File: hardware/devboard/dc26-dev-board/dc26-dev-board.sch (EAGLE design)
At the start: 88 parts, among them CN1 JST, IC1 STM32F411RET6, M10 STM32-Breakout-2, U1 ESP-WROOM-32, Y1 ABL-8.000MHZ-B2

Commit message: ready for review again.
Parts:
- renumbered U$3 to CHARGING_CIRCUT, U$6 to RESET_BUTTON
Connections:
- net PA10 renamed USART1_RX
- net PA9 renamed USART1_TX

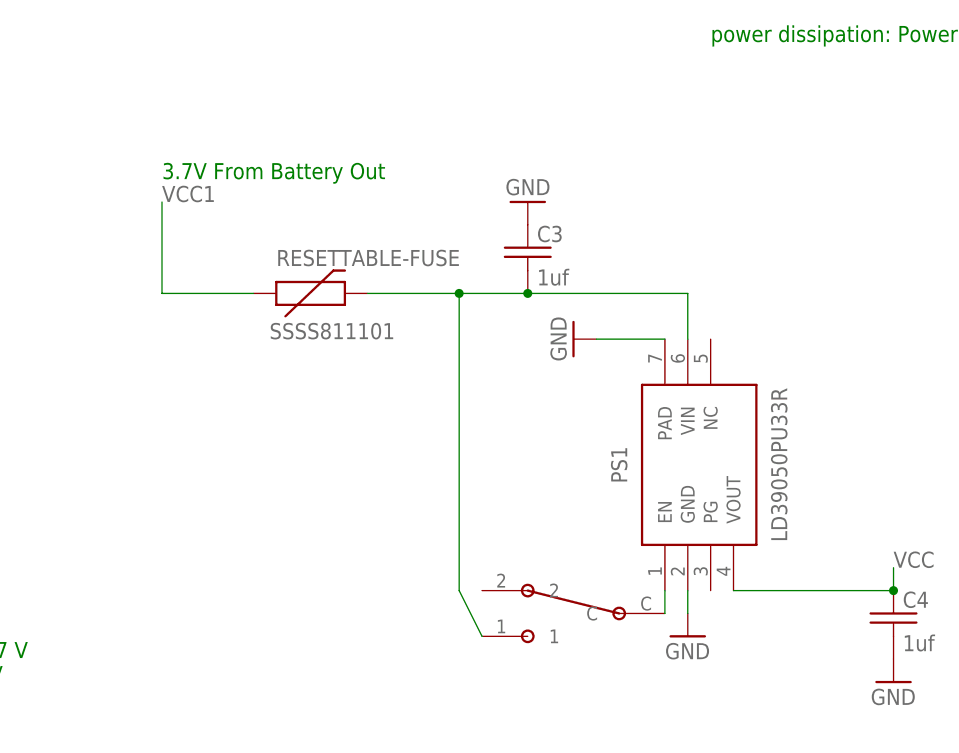
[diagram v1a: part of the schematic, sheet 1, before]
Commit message: swapped out voltage regulator for one that supports 1A rather than just .5A
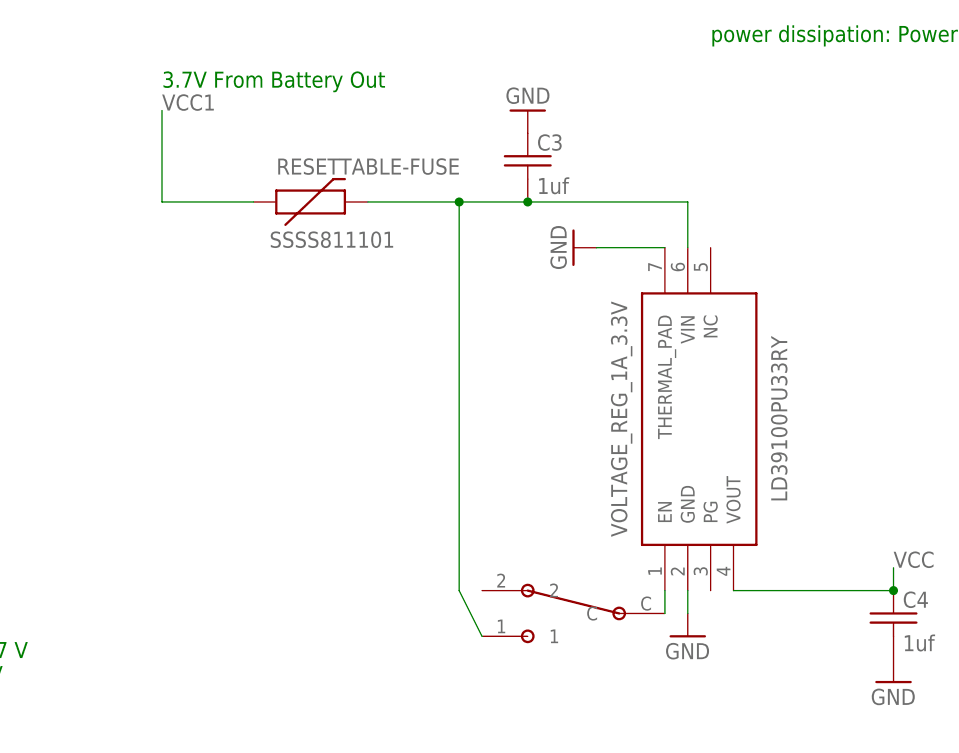
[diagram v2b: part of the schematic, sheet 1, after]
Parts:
- removed PS1: LD39050PU33R, dc-26:LD39050PU33R
- added VOLTAGE_REG_1A_3.3V: LD39100PU33RY, dc-26:LD39100PU33RY
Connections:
- net GND: now also VOLTAGE_REG_1A_3.3V.GND, VOLTAGE_REG_1A_3.3V.THERMAL_PAD; no longer PS1.GND, PS1.PAD
- net VCC: now also VOLTAGE_REG_1A_3.3V.VOUT; no longer PS1.VOUT
- net VIN: now also VOLTAGE_REG_1A_3.3V.VIN; no longer PS1.VIN
- net VIN-EN: now also VOLTAGE_REG_1A_3.3V.EN; no longer PS1.EN
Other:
- moved on the sheet: C3, RESETTABLE-FUSE
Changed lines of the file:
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@@
 <part name="C17" library="dc-26" deviceset="C-US" device="C0805" value="4.7uF"/>
 <part name="GND65" library="dc-26" deviceset="GND" device=""/>
-<part name="PS1" library="dc-26" deviceset="LD39050PU33R" device=""/>
 <part name="GND7" library="dc-26" deviceset="GND" device=""/>
 <part name="R5" library="dc-26" deviceset="RESISTOR" device="0805-RES" value="10K"/>
@@
 <part name="GND69" library="dc-26" deviceset="GND" device=""/>
 <part name="R8" library="dc-26" deviceset="RESISTOR" device="0805-RES" value="4K7"/>
+<part name="VOLTAGE_REG_1A_3.3V" library="dc-26" deviceset="LD39100PU33RY" device=""/>
 </parts>
 <sheets>
@@
 <text x="43.18" y="91.44" size="1.778" layer="91">Battery, USB, ST-LINK Power Out</text>
 <text x="172.72" y="114.3" size="1.778" layer="91">power dissipation: Power Rule: P = I × V</text>
-<text x="111.76" y="99.06" size="1.778" layer="91">3.7V From Battery Out</text>
+<text x="111.76" y="109.22" size="1.778" layer="91">3.7V From Battery Out</text>
 <text x="81.28" y="43.18" size="1.778" layer="91">VCC0 = 5V
 VCC 1 = 3.7 V
@@
 <instance part="R2" gate="G$1" x="-7.62" y="81.28" rot="R90"/>
 <instance part="R3" gate="G$1" x="27.94" y="71.12" rot="R90"/>
-<instance part="RESETTABLE-FUSE" gate="G$1" x="127" y="86.36"/>
+<instance part="RESETTABLE-FUSE" gate="G$1" x="127" y="96.52"/>
 <instance part="U$5" gate="G$1" x="157.48" y="50.8"/>
-<instance part="C3" gate="G$1" x="152.4" y="91.44"/>
+<instance part="C3" gate="G$1" x="152.4" y="101.6"/>
 <instance part="C4" gate="G$1" x="193.04" y="50.8"/>
-<instance part="GND6" gate="1" x="152.4" y="96.52" rot="R180"/>
+<instance part="GND6" gate="1" x="152.4" y="106.68" rot="R180"/>
 <instance part="GND" gate="1" x="193.04" y="43.18"/>
 <instance part="GND8" gate="1" x="170.18" y="48.26"/>
-<instance part="PS1" gate="G$1" x="167.64" y="53.34" rot="R90"/>
-<instance part="GND7" gate="1" x="157.48" y="81.28" rot="R270"/>
+<instance part="GND7" gate="1" x="157.48" y="91.44" rot="R270"/>
 <instance part="U$2" gate="G$1" x="27.94" y="33.02" rot="R180"/>
 <instance part="U$4" gate="G$1" x="15.24" y="2.54"/>
 <instance part="GND5" gate="1" x="43.18" y="-15.24"/>
 <instance part="GND9" gate="1" x="43.18" y="40.64" rot="R180"/>
+<instance part="VOLTAGE_REG_1A_3.3V" gate="G$1" x="167.64" y="53.34" rot="R90"/>
 </instances>
 <busses>
@@
 </segment>
 <segment>
-<pinref part="PS1" gate="G$1" pin="GND"/>
 <wire x1="170.18" y1="53.34" x2="170.18" y2="50.8" width="0.1524" layer="91"/>
 <pinref part="GND8" gate="1" pin="GND"/>
-</segment>
-<segment>
-<pinref part="PS1" gate="G$1" pin="PAD"/>
-<wire x1="167.64" y1="81.28" x2="160.02" y2="81.28" width="0.1524" layer="91"/>
-<pinref part="GND7" gate="1" pin="GND"/>
+<pinref part="VOLTAGE_REG_1A_3.3V" gate="G$1" pin="GND"/>
 </segment>
 <segment>
@@
 <wire x1="43.18" y1="30.48" x2="43.18" y2="38.1" width="0.1524" layer="91"/>
 <pinref part="GND9" gate="1" pin="GND"/>
+</segment>
+<segment>
+<pinref part="VOLTAGE_REG_1A_3.3V" gate="G$1" pin="THERMAL_PAD"/>
+<pinref part="GND7" gate="1" pin="GND"/>
+<wire x1="167.64" y1="91.44" x2="160.02" y2="91.44" width="0.1524" layer="91"/>
 </segment>
 </net>
@@
 <segment>
 <pinref part="RESETTABLE-FUSE" gate="G$1" pin="1"/>
-<wire x1="111.76" y1="96.52" x2="111.76" y2="86.36" width="0.1524" layer="91"/>
-<wire x1="111.76" y1="86.36" x2="121.92" y2="86.36" width="0.1524" layer="91"/>
-<label x="111.76" y="96.52" size="1.778" layer="95"/>
+<wire x1="111.76" y1="106.68" x2="111.76" y2="96.52" width="0.1524" layer="91"/>
+<wire x1="111.76" y1="96.52" x2="121.92" y2="96.52" width="0.1524" layer="91"/>
+<label x="111.76" y="106.68" size="1.778" layer="95"/>
 </segment>
 </net>
@@
 <pinref part="C3" gate="G$1" pin="2"/>
 <pinref part="RESETTABLE-FUSE" gate="G$1" pin="2"/>
-<wire x1="152.4" y1="86.36" x2="144.78" y2="86.36" width="0.1524" layer="91"/>
-<junction x="152.4" y="86.36"/>
+<wire x1="152.4" y1="96.52" x2="144.78" y2="96.52" width="0.1524" layer="91"/>
+<junction x="152.4" y="96.52"/>
 <pinref part="U$5" gate="G$1" pin="1"/>
-<wire x1="144.78" y1="86.36" x2="134.62" y2="86.36" width="0.1524" layer="91"/>
+<wire x1="144.78" y1="96.52" x2="134.62" y2="96.52" width="0.1524" layer="91"/>
 <wire x1="147.32" y1="48.26" x2="144.78" y2="53.34" width="0.1524" layer="91"/>
-<wire x1="144.78" y1="53.34" x2="144.78" y2="86.36" width="0.1524" layer="91"/>
-<junction x="144.78" y="86.36"/>
-<pinref part="PS1" gate="G$1" pin="VIN"/>
-<wire x1="152.4" y1="86.36" x2="170.18" y2="86.36" width="0.1524" layer="91"/>
-<wire x1="170.18" y1="86.36" x2="170.18" y2="81.28" width="0.1524" layer="91"/>
+<wire x1="144.78" y1="53.34" x2="144.78" y2="96.52" width="0.1524" layer="91"/>
+<junction x="144.78" y="96.52"/>
+<wire x1="152.4" y1="96.52" x2="170.18" y2="96.52" width="0.1524" layer="91"/>
+<pinref part="VOLTAGE_REG_1A_3.3V" gate="G$1" pin="VIN"/>
+<wire x1="170.18" y1="91.44" x2="170.18" y2="96.52" width="0.1524" layer="91"/>
 </segment>
 </net>
@@
 <wire x1="193.04" y1="53.34" x2="193.04" y2="55.88" width="0.1524" layer="91"/>
 <label x="193.04" y="55.88" size="1.778" layer="95"/>
-<pinref part="PS1" gate="G$1" pin="VOUT"/>
 <wire x1="175.26" y1="53.34" x2="193.04" y2="53.34" width="0.1524" layer="91"/>
 <junction x="193.04" y="53.34"/>
+<pinref part="VOLTAGE_REG_1A_3.3V" gate="G$1" pin="VOUT"/>
 </segment>
 </net>
@@
 <segment>
 <pinref part="U$5" gate="G$1" pin="C"/>
-<pinref part="PS1" gate="G$1" pin="EN"/>
 <wire x1="167.64" y1="50.8" x2="167.64" y2="53.34" width="0.1524" layer="91"/>
-</segment>
-</net>
+<pinref part="VOLTAGE_REG_1A_3.3V" gate="G$1" pin="EN"/>
+</segment>
+</net>

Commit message: inital board layout
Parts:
- renumbered ESP32-PROGRAM-HEADER to ESP32PH, U$2 to USB, U$4 to LINK1, VOLTAGE_REG_1A_3.3V to VDO
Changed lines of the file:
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@@
 <part name="C1" library="dc-26" deviceset="C-US" device="C0805" value="4.7uF"/>
 <part name="C2" library="dc-26" deviceset="C-US" device="C0805" value="4.7uf"/>
-<part name="U$2" library="dc-26" deviceset="DX4R005JJ2" device="DX4R005JJ2"/>
+<part name="USB" library="dc-26" deviceset="DX4R005JJ2" device="DX4R005JJ2"/>
 <part name="CHARGING_CIRCUT" library="dc-26" deviceset="DS21984E" device="" value="MCP73831"/>
 <part name="GND1" library="dc-26" deviceset="GND" device=""/>
@@
 <part name="GND4" library="dc-26" deviceset="GND" device=""/>
 <part name="LED1" library="dc-26" deviceset="LED" device="1206" value="MF-LED-0603-GREEN"/>
-<part name="U$4" library="dc-26" deviceset="STLINK-V2-CONNECTOR" device=""/>
+<part name="LINK1" library="dc-26" deviceset="STLINK-V2-CONNECTOR" device=""/>
 <part name="GND5" library="dc-26" deviceset="GND" device=""/>
 <part name="RESETTABLE-FUSE" library="dc-26" deviceset="PTC" device="SMD" value="SSSS811101"/>
@@
 <part name="C13" library="dc-26" deviceset="C-US" device="C0805" value="10uF"/>
 <part name="GND13" library="dc-26" deviceset="GND" device=""/>
-<part name="ESP32-PROGRAM-HEADER" library="dc-26" deviceset="SERIAL_4" device=""/>
+<part name="ESP32PH" library="dc-26" deviceset="SERIAL_4" device=""/>
 <part name="Z1" library="dc-26" deviceset="CMDZ3L3_TR" device=""/>
 <part name="GND14" library="dc-26" deviceset="GND" device=""/>
@@
 <part name="GND69" library="dc-26" deviceset="GND" device=""/>
 <part name="R8" library="dc-26" deviceset="RESISTOR" device="0805-RES" value="4K7"/>
-<part name="VOLTAGE_REG_1A_3.3V" library="dc-26" deviceset="LD39100PU33RY" device=""/>
+<part name="VDO" library="dc-26" deviceset="LD39100PU33RY" device=""/>
 </parts>
 <sheets>
@@
 <instance part="GND8" gate="1" x="170.18" y="48.26"/>
 <instance part="GND7" gate="1" x="157.48" y="91.44" rot="R270"/>
-<instance part="U$2" gate="G$1" x="27.94" y="33.02" rot="R180"/>
-<instance part="U$4" gate="G$1" x="15.24" y="2.54"/>
+<instance part="USB" gate="G$1" x="27.94" y="33.02" rot="R180"/>
+<instance part="LINK1" gate="G$1" x="15.24" y="2.54"/>
 <instance part="GND5" gate="1" x="43.18" y="-15.24"/>
 <instance part="GND9" gate="1" x="43.18" y="40.64" rot="R180"/>
-<instance part="VOLTAGE_REG_1A_3.3V" gate="G$1" x="167.64" y="53.34" rot="R90"/>
+<instance part="VDO" gate="G$1" x="167.64" y="53.34" rot="R90"/>
 </instances>
 <busses>
@@
 <wire x1="170.18" y1="53.34" x2="170.18" y2="50.8" width="0.1524" layer="91"/>
 <pinref part="GND8" gate="1" pin="GND"/>
-<pinref part="VOLTAGE_REG_1A_3.3V" gate="G$1" pin="GND"/>
-</segment>
-<segment>
-<pinref part="U$4" gate="G$1" pin="GND"/>
+<pinref part="VDO" gate="G$1" pin="GND"/>
+</segment>
+<segment>
+<pinref part="LINK1" gate="G$1" pin="GND"/>
 <wire x1="25.4" y1="-7.62" x2="43.18" y2="-7.62" width="0.1524" layer="91"/>
 <wire x1="43.18" y1="-7.62" x2="43.18" y2="-12.7" width="0.1524" layer="91"/>
@@
 </segment>
 <segment>
-<pinref part="U$2" gate="G$1" pin="GND"/>
+<pinref part="USB" gate="G$1" pin="GND"/>
 <wire x1="33.02" y1="30.48" x2="43.18" y2="30.48" width="0.1524" layer="91"/>
 <wire x1="43.18" y1="30.48" x2="43.18" y2="38.1" width="0.1524" layer="91"/>
@@
 </segment>
 <segment>
-<pinref part="VOLTAGE_REG_1A_3.3V" gate="G$1" pin="THERMAL_PAD"/>
+<pinref part="VDO" gate="G$1" pin="THERMAL_PAD"/>
 <pinref part="GND7" gate="1" pin="GND"/>
 <wire x1="167.64" y1="91.44" x2="160.02" y2="91.44" width="0.1524" layer="91"/>
@@
 </segment>
 <segment>
-<pinref part="U$4" gate="G$1" pin="VCC"/>
+<pinref part="LINK1" gate="G$1" pin="VCC"/>
 <wire x1="25.4" y1="0" x2="43.18" y2="0" width="0.1524" layer="91"/>
 <wire x1="43.18" y1="0" x2="43.18" y2="5.08" width="0.1524" layer="91"/>
@@
 </segment>
 <segment>
-<pinref part="U$2" gate="G$1" pin="+5V"/>
+<pinref part="USB" gate="G$1" pin="+5V"/>
 <wire x1="33.02" y1="20.32" x2="40.64" y2="20.32" width="0.1524" layer="91"/>
 <label x="40.64" y="20.32" size="1.778" layer="95"/>
@@
 <junction x="144.78" y="96.52"/>
 <wire x1="152.4" y1="96.52" x2="170.18" y2="96.52" width="0.1524" layer="91"/>
-<pinref part="VOLTAGE_REG_1A_3.3V" gate="G$1" pin="VIN"/>
+<pinref part="VDO" gate="G$1" pin="VIN"/>
 <wire x1="170.18" y1="91.44" x2="170.18" y2="96.52" width="0.1524" layer="91"/>
 </segment>
@@
 <wire x1="175.26" y1="53.34" x2="193.04" y2="53.34" width="0.1524" layer="91"/>
 <junction x="193.04" y="53.34"/>
-<pinref part="VOLTAGE_REG_1A_3.3V" gate="G$1" pin="VOUT"/>
+<pinref part="VDO" gate="G$1" pin="VOUT"/>
 </segment>
 </net>
@@
 <pinref part="U$5" gate="G$1" pin="C"/>
 <wire x1="167.64" y1="50.8" x2="167.64" y2="53.34" width="0.1524" layer="91"/>
-<pinref part="VOLTAGE_REG_1A_3.3V" gate="G$1" pin="EN"/>
+<pinref part="VDO" gate="G$1" pin="EN"/>
 </segment>
 </net>
 <net name="SYS_JTCK_SWCLK" class="0">
 <segment>
-<pinref part="U$4" gate="G$1" pin="SWDCLK"/>
+<pinref part="LINK1" gate="G$1" pin="SWDCLK"/>
 <wire x1="25.4" y1="-5.08" x2="40.64" y2="-5.08" width="0.1524" layer="91"/>
 <label x="45.72" y="-5.08" size="1.778" layer="95"/>
@@
 <net name="SYS_JTMS_SWDIO" class="0">
 <segment>
-<pinref part="U$4" gate="G$1" pin="SWDIO"/>
+<pinref part="LINK1" gate="G$1" pin="SWDIO"/>
 <wire x1="25.4" y1="-2.54" x2="38.1" y2="-2.54" width="0.1524" layer="91"/>
 <label x="45.72" y="-2.54" size="1.778" layer="95"/>
@@
 <net name="USB_DM" class="0">
 <segment>
-<pinref part="U$2" gate="G$1" pin="D+"/>
+<pinref part="USB" gate="G$1" pin="D+"/>
 <wire x1="33.02" y1="25.4" x2="48.26" y2="25.4" width="0.1524" layer="91"/>
 <label x="50.8" y="25.4" size="1.778" layer="95"/>
@@
 <net name="USB_DP" class="0">
 <segment>
-<pinref part="U$2" gate="G$1" pin="D-"/>
+<pinref part="USB" gate="G$1" pin="D-"/>
 <wire x1="33.02" y1="22.86" x2="48.26" y2="22.86" width="0.1524" layer="91"/>
 <label x="50.8" y="22.86" size="1.778" layer="95"/>
@@
 <instance part="C13" gate="G$1" x="-43.18" y="53.34"/>
 <instance part="GND13" gate="1" x="-43.18" y="43.18"/>
-<instance part="ESP32-PROGRAM-HEADER" gate="G$1" x="-38.1" y="-15.24" rot="R90"/>
+<instance part="ESP32PH" gate="G$1" x="-38.1" y="-15.24" rot="R90"/>
 <instance part="Z1" gate="G$1" x="50.8" y="-12.7" rot="R90"/>
 <instance part="GND14" gate="1" x="-25.4" y="71.12" rot="R180"/>
@@
 </segment>
 <segment>
-<pinref part="ESP32-PROGRAM-HEADER" gate="G$1" pin="GND"/>
+<pinref part="ESP32PH" gate="G$1" pin="GND"/>
 <wire x1="-33.02" y1="-7.62" x2="-33.02" y2="-2.54" width="0.1524" layer="91"/>
 <label x="-33.02" y="-2.54" size="1.778" layer="95" rot="R90"/>
@@
 <net name="VCC" class="0">
 <segment>
-<pinref part="ESP32-PROGRAM-HEADER" gate="G$1" pin="VCC"/>
+<pinref part="ESP32PH" gate="G$1" pin="VCC"/>
 <wire x1="-40.64" y1="-7.62" x2="-40.64" y2="-2.54" width="0.1524" layer="91"/>
 <label x="-40.64" y="-2.54" size="1.778" layer="95" rot="R90"/>
@@
 <net name="ESP-RX" class="0">
 <segment>
-<pinref part="ESP32-PROGRAM-HEADER" gate="G$1" pin="RX"/>
+<pinref part="ESP32PH" gate="G$1" pin="RX"/>
 <wire x1="-38.1" y1="-7.62" x2="-38.1" y2="-2.54" width="0.1524" layer="91"/>
 <label x="-38.1" y="-2.54" size="1.778" layer="95" rot="R90"/>
@@
 </segment>
 <segment>
-<pinref part="ESP32-PROGRAM-HEADER" gate="G$1" pin="TX"/>
+<pinref part="ESP32PH" gate="G$1" pin="TX"/>
 <wire x1="-35.56" y1="-7.62" x2="-35.56" y2="-2.54" width="0.1524" layer="91"/>
 <label x="-35.56" y="-2.54" size="1.778" layer="95" rot="R90"/>

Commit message: auto routed boardwith some minor vcc changes by hand.
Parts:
- added U$2: CMD_C0DE_LOGO, dc-26:CMD_C0DE_LOGO
- added U$3: DARKNET_DD, dc-26:DARKNET_DD
- added U$4: DARKNET_NN, dc-26:DARKNET_NN
- added U$6: KRUX_LOGO, dc-26:KRUX_LOGO
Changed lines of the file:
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@@
 <part name="R8" library="dc-26" deviceset="RESISTOR" device="0805-RES" value="4K7"/>
 <part name="VDO" library="dc-26" deviceset="LD39100PU33RY" device=""/>
+<part name="U$2" library="dc-26" deviceset="CMD_C0DE_LOGO" device=""/>
+<part name="U$3" library="dc-26" deviceset="DARKNET_D" device="D"/>
+<part name="U$4" library="dc-26" deviceset="DARKNET_N" device="N"/>
+<part name="U$6" library="dc-26" deviceset="KRUX_LOGO" device=""/>
 </parts>
 <sheets>
@@
 </nets>
 </sheet>
+<sheet>
+<plain>
+</plain>
+<instances>
+<instance part="U$2" gate="G$1" x="10.16" y="88.9"/>
+<instance part="U$3" gate="G$1" x="27.94" y="86.36"/>
+<instance part="U$4" gate="G$1" x="35.56" y="86.36"/>
+<instance part="U$6" gate="G$1" x="30.48" y="71.12"/>
+</instances>
+<busses>
+</busses>
+<nets>
+</nets>
+</sheet>

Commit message: minor fixed of part naming and added todo file
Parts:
- P1: value SWITCH_SPDT -> SSSS811101
- renumbered U$5 to P1
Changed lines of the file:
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@@
 <part name="GND5" library="dc-26" deviceset="GND" device=""/>
 <part name="RESETTABLE-FUSE" library="dc-26" deviceset="PTC" device="SMD" value="SSSS811101"/>
-<part name="U$5" library="dc-26" deviceset="SWITCH_SPDT" device=""/>
+<part name="P1" library="dc-26" deviceset="SWITCH_SPDT" device="" value="SSSS811101"/>
 <part name="R2" library="dc-26" deviceset="RESISTOR" device="0805-RES" value="470"/>
 <part name="R3" library="dc-26" deviceset="RESISTOR" device="0805-RES" value="2k"/>
@@
 <instance part="R3" gate="G$1" x="27.94" y="71.12" rot="R90"/>
 <instance part="RESETTABLE-FUSE" gate="G$1" x="127" y="96.52"/>
-<instance part="U$5" gate="G$1" x="157.48" y="50.8"/>
+<instance part="P1" gate="G$1" x="157.48" y="50.8"/>
 <instance part="C3" gate="G$1" x="152.4" y="101.6"/>
 <instance part="C4" gate="G$1" x="193.04" y="50.8"/>
@@
 <wire x1="152.4" y1="96.52" x2="144.78" y2="96.52" width="0.1524" layer="91"/>
 <junction x="152.4" y="96.52"/>
-<pinref part="U$5" gate="G$1" pin="1"/>
+<pinref part="P1" gate="G$1" pin="1"/>
 <wire x1="144.78" y1="96.52" x2="134.62" y2="96.52" width="0.1524" layer="91"/>
 <wire x1="147.32" y1="48.26" x2="144.78" y2="53.34" width="0.1524" layer="91"/>
@@
 <net name="VIN-EN" class="0">
 <segment>
-<pinref part="U$5" gate="G$1" pin="C"/>
+<pinref part="P1" gate="G$1" pin="C"/>
 <wire x1="167.64" y1="50.8" x2="167.64" y2="53.34" width="0.1524" layer="91"/>
 <pinref part="VDO" gate="G$1" pin="EN"/>
